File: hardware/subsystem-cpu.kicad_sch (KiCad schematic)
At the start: 1 part, among them J3 MicroMod-M.2E

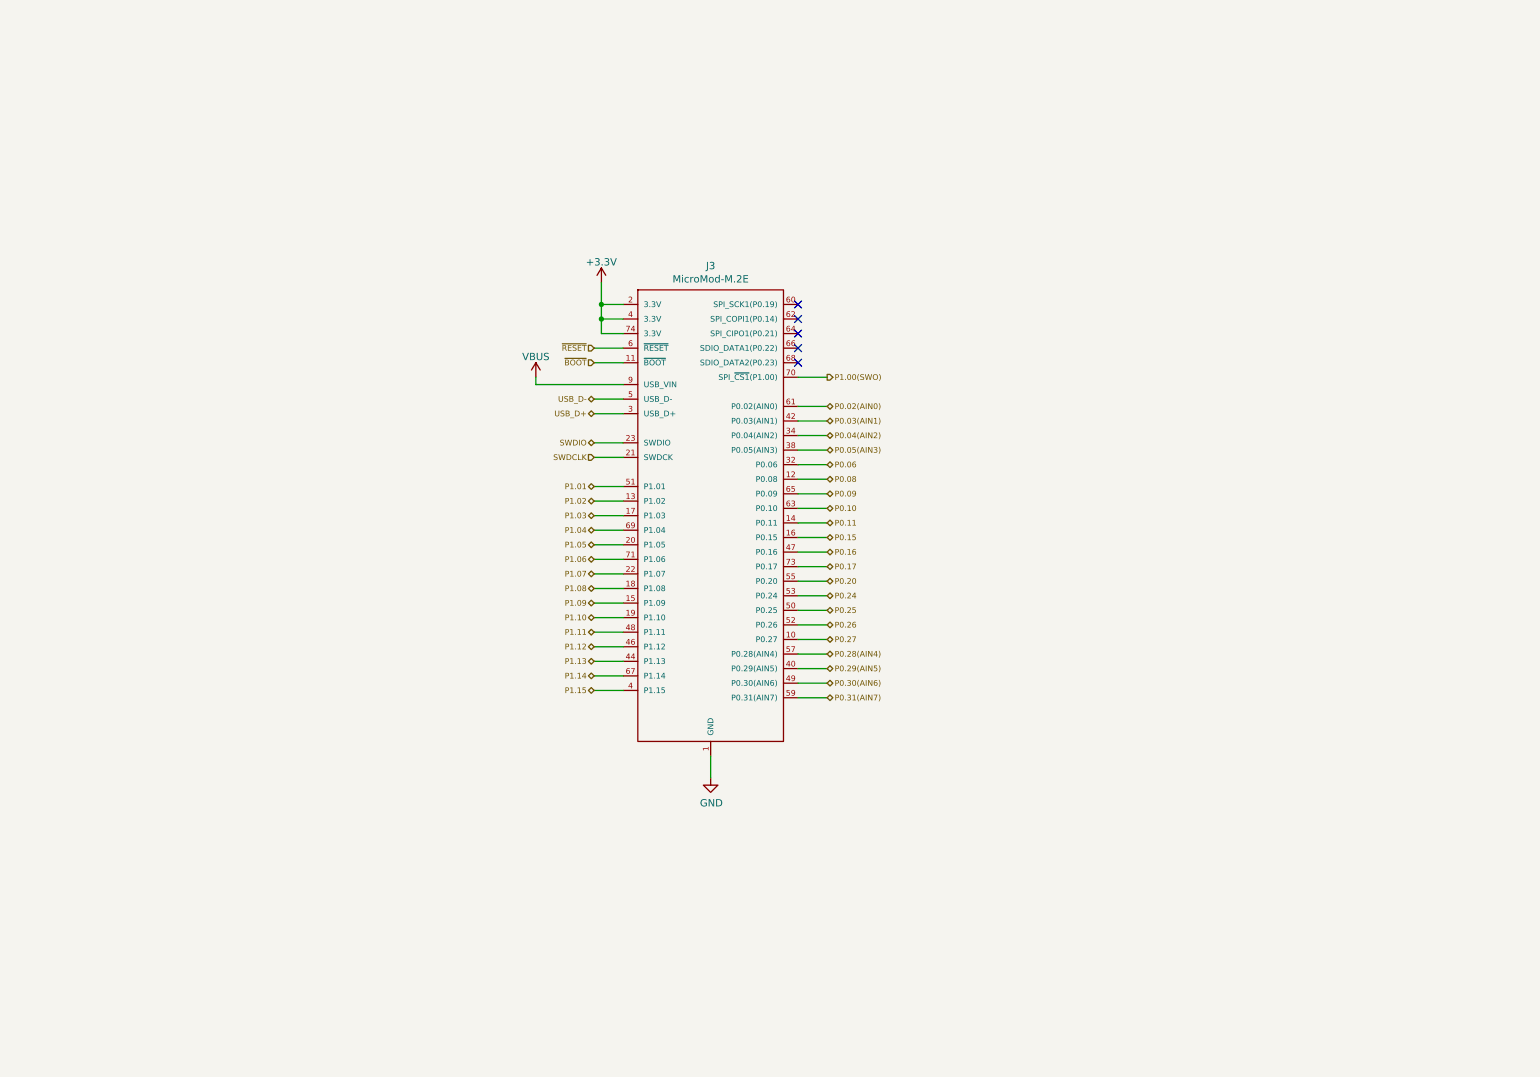
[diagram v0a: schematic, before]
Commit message: hardware: first nRF52840 raw tries
The current schematic should (in theory) be a complete setup for the
nRF52840 chip with power and everything.

In the footprint first routing attempts have been made, but this has
been without real success for now, especially as the nRF52840 is a hell
of a chip to implement. Ignoring the whole "need to do own RF" here,
it's almost impossible to get the inner pins out from under the chip
without paying extra for either via-in-pads or precision milling.

I'll leave this commit here for an exemplary routing of (some) inner
GPIO pins off the nRF52840 while presumably being in spec of JLCPCBs
capabilities. I want this project to come to an end, so I'll step away
from implementing my own nRF52840, and buy a carrier module with it
instead.

And yeah - RF stuff is magic and mostly consists of dark incantations.
The major advantage of buying a carrier board that already does the RF
for me, is that I have fewer requirements on the PCB manufacturer and
people can just manufacture it with their favorite producer.

Signed-off-by: Sophie Friedrich <dev@flowerpot.me>
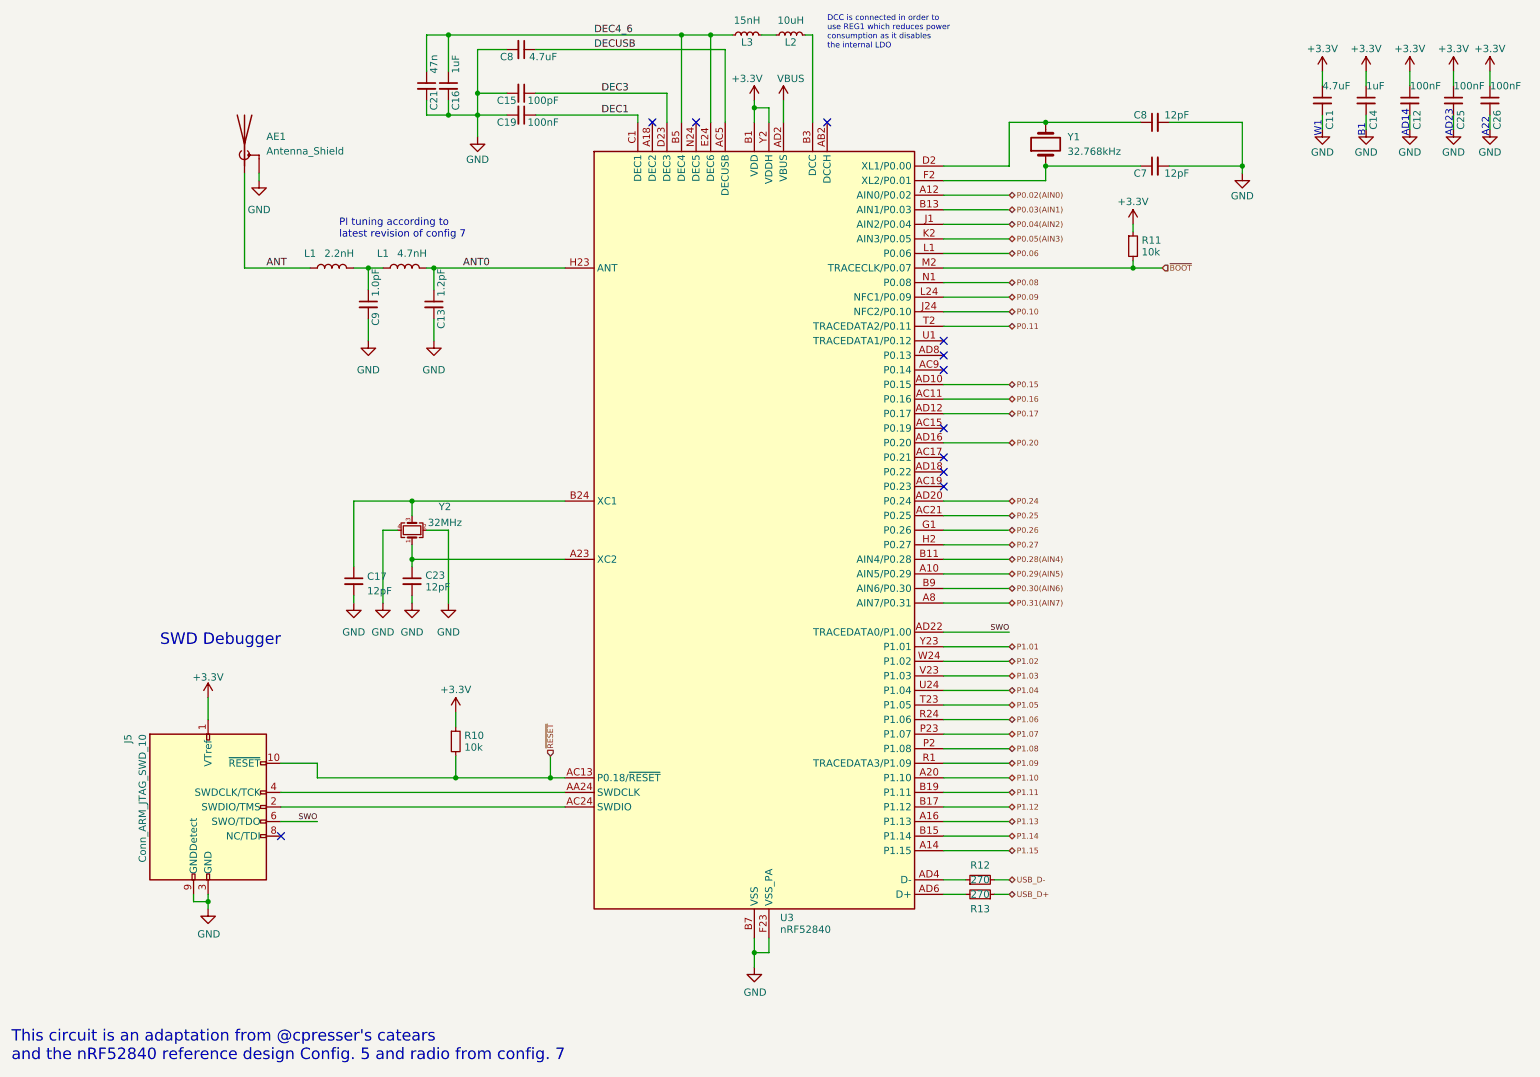
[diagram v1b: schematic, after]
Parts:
- removed J3: MicroMod-M.2E, SparkFun MicroMod:M.2-CONNECTOR-E, symbol custom_footprints:MicroMod-M.2E
- added AE1: Antenna_Shield, RF_Antenna:Texas_SWRA117D_2.4GHz_Right, symbol Device:Antenna_Shield
- added C11, C8: 4.7uF, Capacitor_SMD:C_0603_1608Metric_Pad1.08x0.95mm_HandSolder, symbol Device:C_Small
- added C12, C19, C25, C26: 100nF, Capacitor_SMD:C_0603_1608Metric_Pad1.08x0.95mm_HandSolder, symbol Device:C_Small
- added C13: 1.2pF, Capacitor_SMD:C_0603_1608Metric_Pad1.08x0.95mm_HandSolder, symbol Device:C_Small
- added C14, C16: 1uF, Capacitor_SMD:C_0603_1608Metric_Pad1.08x0.95mm_HandSolder, symbol Device:C_Small
- added C15: 100pF, Capacitor_SMD:C_0603_1608Metric_Pad1.08x0.95mm_HandSolder, symbol Device:C_Small
- added C17, C23, C7, C8: 12pF, Capacitor_SMD:C_0603_1608Metric_Pad1.08x0.95mm_HandSolder, symbol Device:C_Small
- added C21: 47n, Capacitor_SMD:C_0603_1608Metric_Pad1.08x0.95mm_HandSolder, symbol Device:C_Small
- added C9: 1.0pF, Capacitor_SMD:C_0603_1608Metric_Pad1.08x0.95mm_HandSolder, symbol Device:C_Small
- added J5: Conn_ARM_JTAG_SWD_10, Connector_PinHeader_1.27mm:PinHeader_2x05_P1.27mm_Vertical_SMD, symbol Connector:Conn_ARM_JTAG_SWD_10
- added L1: 2.2nH, Inductor_SMD:L_0603_1608Metric, symbol Device:L
- added L1: 4.7nH, Inductor_SMD:L_0603_1608Metric, symbol Device:L
- added L2: 10uH, Inductor_SMD:L_0603_1608Metric, symbol Device:L_Small
- added L3: 15nH, Inductor_SMD:L_0603_1608Metric, symbol Device:L_Small
- added R10, R11: 10k, Capacitor_SMD:C_0603_1608Metric_Pad1.08x0.95mm_HandSolder, symbol Device:R_Small
- added R12, R13: 270, Capacitor_SMD:C_0603_1608Metric_Pad1.08x0.95mm_HandSolder, symbol Device:R_Small
- added U3: nRF52840, Package_DFN_QFN:Nordic_AQFN-73-1EP_7x7mm_P0.5mm, symbol MCU_Nordic:nRF52840
- added Y1: 32.768kHz, Capacitor_SMD:C_0603_1608Metric_Pad1.08x0.95mm_HandSolder, symbol Device:Crystal
- added Y2: 32MHz, Crystal:Crystal_SMD_2520-4Pin_2.5x2.0mm, symbol Device:Crystal_GND24_Small
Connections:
- net GND: now also AE1.2 (Shield), C11.2, C12.2, C13.2, C14.2, C15.2, C16.2, C17.2, C19.2, C21.2, C23.2, C25.2, C26.2, C7.2, C8.2, C8.2, C9.2, J5.3 (GND), J5.5 (GND), J5.9 (GNDDetect), U3.B7 (VSS), U3.EP (VSS), U3.F23 (VSS_PA), Y2.2, Y2.4
- net P0.02(AIN0): now also U3.A12 (AIN0/P0.02)
- net P0.03(AIN1): now also U3.B13 (AIN1/P0.03)
- net P0.04(AIN2): now also U3.J1 (AIN2/P0.04)
- net P0.05(AIN3): now also U3.K2 (AIN3/P0.05)
- net P0.06: now also U3.L1 (P0.06)
- net P0.08: now also U3.N1 (P0.08)
- net P0.09: now also U3.L24 (NFC1/P0.09)
- net P0.10: now also U3.J24 (NFC2/P0.10)
- net P0.11: now also U3.T2 (TRACEDATA2/P0.11)
- net P0.15: now also U3.AD10 (P0.15)
- net P0.16: now also U3.AC11 (P0.16)
- net P0.17: now also U3.AD12 (P0.17)
- net P0.20: now also U3.AD16 (P0.20)
- net P0.24: now also U3.AD20 (P0.24)
- net P0.25: now also U3.AC21 (P0.25)
- net P0.26: now also U3.G1 (P0.26)
- net P0.27: now also U3.H2 (P0.27)
- net P0.28(AIN4): now also U3.B11 (AIN4/P0.28)
- net P0.29(AIN5): now also U3.A10 (AIN5/P0.29)
- net P0.30(AIN6): now also U3.B9 (AIN6/P0.30)
- net P0.31(AIN7): now also U3.A8 (AIN7/P0.31)
- net P1.01: now also U3.Y23 (P1.01)
- net P1.02: now also U3.W24 (P1.02)
- net P1.03: now also U3.V23 (P1.03)
- net P1.04: now also U3.U24 (P1.04)
- net P1.05: now also U3.T23 (P1.05)
- net P1.06: now also U3.R24 (P1.06)
- net P1.07: now also U3.P23 (P1.07)
- net P1.08: now also U3.P2 (P1.08)
- net P1.09: now also U3.R1 (TRACEDATA3/P1.09)
- net P1.10: now also U3.A20 (P1.10)
- net P1.11: now also U3.B19 (P1.11)
- net P1.12: now also U3.B17 (P1.12)
- net P1.13: now also U3.A16 (P1.13)
- net P1.14: now also U3.B15 (P1.14)
- net P1.15: now also U3.A14 (P1.15)
- net USB_D+: now also R13.1
- net USB_D-: now also R12.2
- net VBUS: now also U3.AD2 (VBUS)
- net ~{BOOT}: now also R11.2, U3.M2 (TRACECLK/P0.07)
- net ~{RESET}: now also J5.10 (~{RESET}), R10.2, U3.AC13 (P0.18/~{RESET})
- new net: C7.1, U3.F2 (XL2/P0.01), Y1.1
- new net: C8.1, U3.D2 (XL1/P0.00), Y1.2
- new net: C17.1, U3.B24 (XC1), Y2.3
- new net: J5.2 (SWDIO/TMS), U3.AC24 (SWDIO)
- new net: J5.4 (SWDCLK/TCK), U3.AA24 (SWDCLK)
- new net: L2.1, L3.2
- new net: L2.2, U3.B3 (DCC)
- new net: C23.1, U3.A23 (XC2), Y2.1
- new net: R12.1, U3.AD4 (D-)
- new net: R13.2, U3.AD6 (D+)
- new net: C9.1, L1.1, L1.2
- new net +3.3V: C11.1, C12.1, C14.1, C25.1, C26.1, J5.1 (VTref), R10.1, R11.1, U3.A22 (VDD), U3.AD14 (VDD), U3.AD23 (VDD), U3.B1 (VDD), U3.W1 (VDD), U3.Y2 (VDDH)
- new net ANT: AE1.1 (A), L1.1
- new net ANT0: C13.1, L1.2, U3.H23 (ANT)
- new net DEC1: C19.1, U3.C1 (DEC1)
- new net DEC3: C15.1, U3.D23 (DEC3)
- new net DEC4_6: C16.1, C21.1, L3.1, U3.B5 (DEC4), U3.E24 (DEC6)
- new net DECUSB: C8.1, U3.AC5 (DECUSB)
- new net SWO: J5.6 (SWO/TDO), U3.AD22 (TRACEDATA0/P1.00)
- no-connect marks 5 -> 11
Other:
- note added: "A22"
- note added: "AD14"
- note added: "AD23"
- note added: "B1"
- note added: "DCC is connected in order to use REG1 which reduces power consumption as it disables the internal LDO"
- note added: "PI tuning according to latest revision of config 7"
- note added: "SWD Debugger"
- note added: "This circuit is an adaptation from @cpresser's catears and the nRF52840 reference design Config. 5 and radio from config. 7"
- note added: "W1"

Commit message: Revert "hardware: first nRF52840 raw tries"
Wanna start from a clean slate. See referenced commit on why I'm doing
this.

This reverts commit 5420c1d1e1bdfd9146d776c48bdd16e2d166426d.
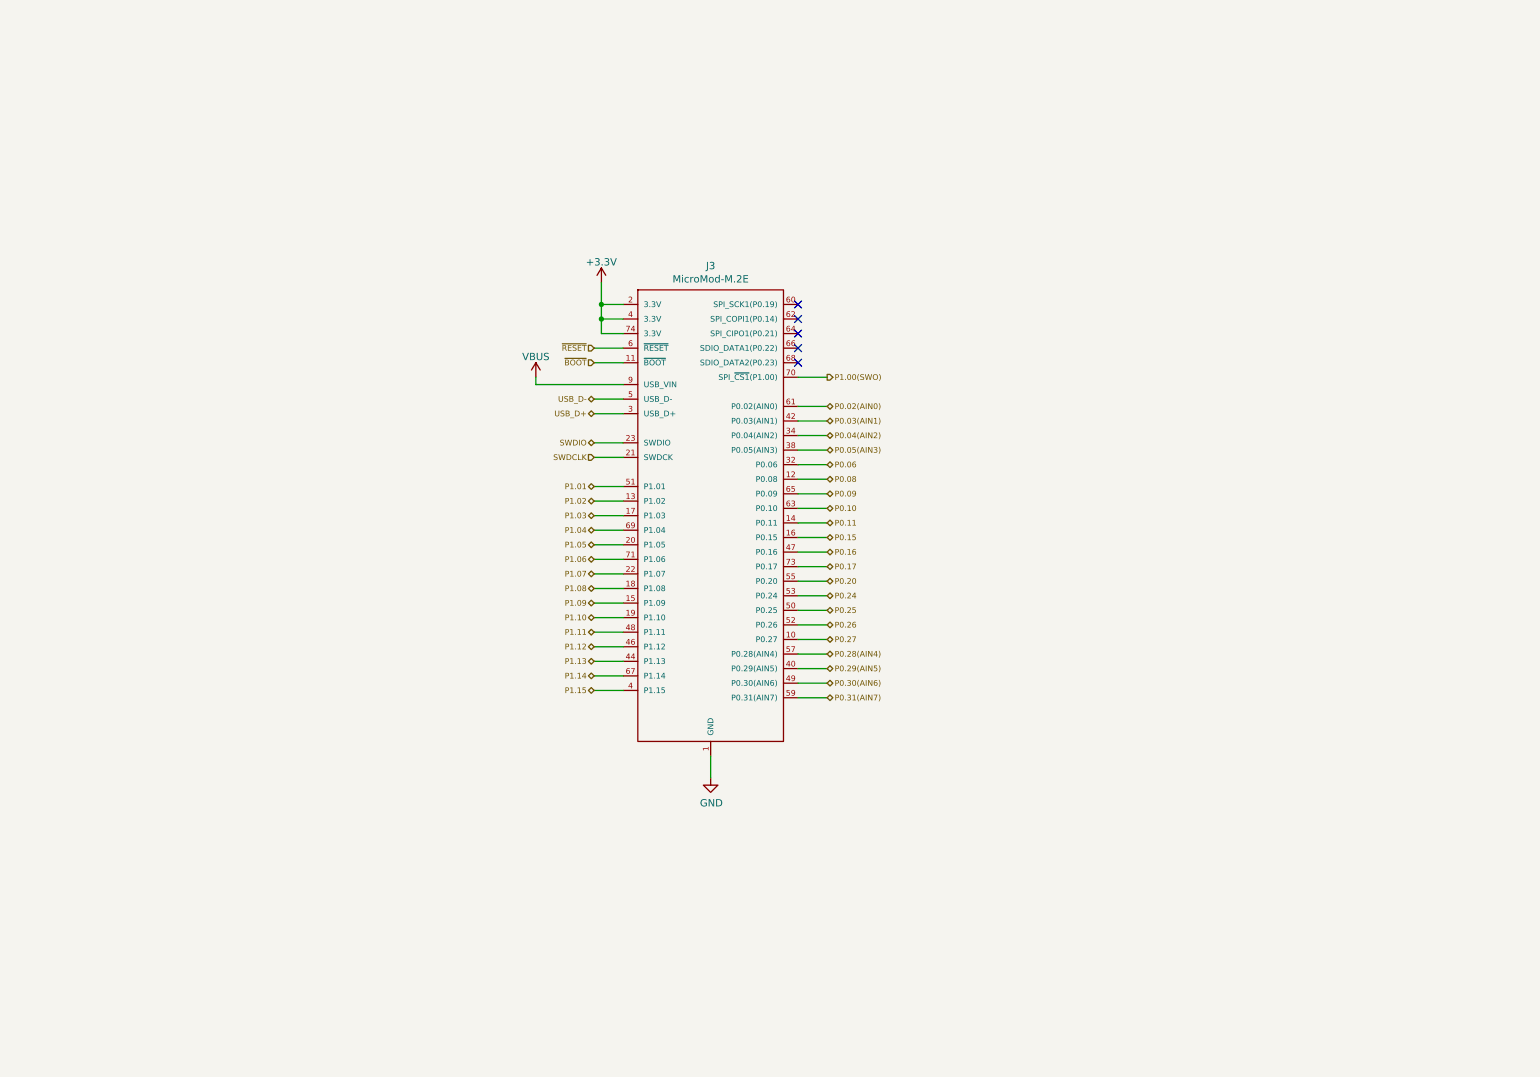
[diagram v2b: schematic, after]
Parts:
- removed AE1: Antenna_Shield, RF_Antenna:Texas_SWRA117D_2.4GHz_Right, symbol Device:Antenna_Shield
- removed C11, C8: 4.7uF, Capacitor_SMD:C_0603_1608Metric_Pad1.08x0.95mm_HandSolder, symbol Device:C_Small
- removed C12, C19, C25, C26: 100nF, Capacitor_SMD:C_0603_1608Metric_Pad1.08x0.95mm_HandSolder, symbol Device:C_Small
- removed C13: 1.2pF, Capacitor_SMD:C_0603_1608Metric_Pad1.08x0.95mm_HandSolder, symbol Device:C_Small
- removed C14, C16: 1uF, Capacitor_SMD:C_0603_1608Metric_Pad1.08x0.95mm_HandSolder, symbol Device:C_Small
- removed C15: 100pF, Capacitor_SMD:C_0603_1608Metric_Pad1.08x0.95mm_HandSolder, symbol Device:C_Small
- removed C17, C23, C7, C8: 12pF, Capacitor_SMD:C_0603_1608Metric_Pad1.08x0.95mm_HandSolder, symbol Device:C_Small
- removed C21: 47n, Capacitor_SMD:C_0603_1608Metric_Pad1.08x0.95mm_HandSolder, symbol Device:C_Small
- removed C9: 1.0pF, Capacitor_SMD:C_0603_1608Metric_Pad1.08x0.95mm_HandSolder, symbol Device:C_Small
- removed J5: Conn_ARM_JTAG_SWD_10, Connector_PinHeader_1.27mm:PinHeader_2x05_P1.27mm_Vertical_SMD, symbol Connector:Conn_ARM_JTAG_SWD_10
- removed L1: 2.2nH, Inductor_SMD:L_0603_1608Metric, symbol Device:L
- removed L1: 4.7nH, Inductor_SMD:L_0603_1608Metric, symbol Device:L
- removed L2: 10uH, Inductor_SMD:L_0603_1608Metric, symbol Device:L_Small
- removed L3: 15nH, Inductor_SMD:L_0603_1608Metric, symbol Device:L_Small
- removed R10, R11: 10k, Capacitor_SMD:C_0603_1608Metric_Pad1.08x0.95mm_HandSolder, symbol Device:R_Small
- removed R12, R13: 270, Capacitor_SMD:C_0603_1608Metric_Pad1.08x0.95mm_HandSolder, symbol Device:R_Small
- removed U3: nRF52840, Package_DFN_QFN:Nordic_AQFN-73-1EP_7x7mm_P0.5mm, symbol MCU_Nordic:nRF52840
- removed Y1: 32.768kHz, Capacitor_SMD:C_0603_1608Metric_Pad1.08x0.95mm_HandSolder, symbol Device:Crystal
- removed Y2: 32MHz, Crystal:Crystal_SMD_2520-4Pin_2.5x2.0mm, symbol Device:Crystal_GND24_Small
- added J3: MicroMod-M.2E, SparkFun MicroMod:M.2-CONNECTOR-E, symbol custom_footprints:MicroMod-M.2E
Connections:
- net GND: now also J3.1 (GND), J3.33 (GND), J3.36 (GND), J3.39 (GND), J3.45 (GND), J3.7 (GND), J3.75 (GND)
- net P0.02(AIN0): now also J3.61 (P0.02(AIN0))
- net P0.03(AIN1): now also J3.42 (P0.03(AIN1))
- net P0.04(AIN2): now also J3.34 (P0.04(AIN2))
- net P0.05(AIN3): now also J3.38 (P0.05(AIN3))
- net P0.06: now also J3.32 (P0.06)
- net P0.08: now also J3.12 (P0.08)
- net P0.09: now also J3.65 (P0.09)
- net P0.10: now also J3.63 (P0.10)
- net P0.11: now also J3.14 (P0.11)
- net P0.15: now also J3.16 (P0.15)
- net P0.16: now also J3.47 (P0.16)
- net P0.17: now also J3.73 (P0.17)
- net P0.20: now also J3.55 (P0.20)
- net P0.24: now also J3.53 (P0.24)
- net P0.25: now also J3.50 (P0.25)
- net P0.26: now also J3.52 (P0.26)
- net P0.27: now also J3.10 (P0.27)
- net P0.28(AIN4): now also J3.57 (P0.28(AIN4))
- net P0.29(AIN5): now also J3.40 (P0.29(AIN5))
- net P0.30(AIN6): now also J3.49 (P0.30(AIN6))
- net P0.31(AIN7): now also J3.59 (P0.31(AIN7))
- net P1.01: now also J3.51 (P1.01)
- net P1.02: now also J3.13 (P1.02)
- net P1.03: now also J3.17 (P1.03)
- net P1.04: now also J3.69 (P1.04)
- net P1.05: now also J3.20 (P1.05)
- net P1.06: now also J3.71 (P1.06)
- net P1.07: now also J3.22 (P1.07)
- net P1.08: now also J3.18 (P1.08)
- net P1.09: now also J3.15 (P1.09)
- net P1.10: now also J3.19 (P1.10)
- net P1.11: now also J3.48 (P1.11)
- net P1.12: now also J3.46 (P1.12)
- net P1.13: now also J3.44 (P1.13)
- net P1.14: now also J3.67 (P1.14)
- net P1.15: now also J3.4 (P1.15)
- net USB_D+: now also J3.3 (USB_D+)
- net USB_D-: now also J3.5 (USB_D-)
- net VBUS: now also J3.9 (USB_VIN)
- net ~{BOOT}: now also J3.11 (~{BOOT})
- net ~{RESET}: now also J3.6 (~{RESET})
- new net +3V3: J3.2 (3.3V), J3.4 (P1.15), J3.74 (3.3V)
- new net P1.00(SWO): J3.70 (SPI_~{CS1}(P1.00))
- new net SWDCLK: J3.21 (SWDCK)
- new net SWDIO: J3.23 (SWDIO)
- no-connect marks 11 -> 5
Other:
- note removed: "A22"
- note removed: "AD14"
- note removed: "AD23"
- note removed: "B1"
- note removed: "DCC is connected in order to use REG1 which reduces power consumption as it disables the internal LDO"
- note removed: "PI tuning according to latest revision of config 7"
- note removed: "SWD Debugger"
- note removed: "This circuit is an adaptation from @cpresser's catears and the nRF52840 reference design Config. 5 and radio from config. 7"
- note removed: "W1"
